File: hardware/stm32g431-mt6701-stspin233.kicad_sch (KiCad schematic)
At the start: 13 parts, among them J101 I2C, J102 UART, J103 CANBUS_IN, J104 CANBUS_OUT, J105 SPI3, J106 CAN TERMINATION, J107 EXT_PWR, J108 MOT_THT, J109 MOT_FPC, U101 SN65HVD230

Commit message: work on layout
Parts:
- removed J103: CANBUS_IN, matei:AVX-009159010061911, symbol Connector_Generic:Conn_01x04
- removed J104: CANBUS_OUT, matei:AVX-009159010061911, symbol Connector_Generic:Conn_01x04
- added H101, H102, H103, H104: M3, MountingHole:MountingHole_3.2mm_M3_DIN965_Pad_TopBottom, symbol Mechanical:MountingHole_Pad
- added J103: CANBUS_IN, matei:AVX-009159010061911, symbol Connector_Generic:Conn_02x05_Top_Bottom
- added J104: CANBUS_OUT, matei:AVX-009159010061911, symbol Connector_Generic:Conn_02x05_Top_Bottom
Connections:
- net +5V: now also J103.8 (Pin_8), J104.3 (Pin_3), J104.4 (Pin_4), J104.8 (Pin_8), J104.9 (Pin_9)
- net CAN_H: now also J103.1 (Pin_1), J103.6 (Pin_6), J104.1 (Pin_1), J104.6 (Pin_6)
- net CAN_L: now also J103.2 (Pin_2), J103.7 (Pin_7), J104.2 (Pin_2), J104.7 (Pin_7)
- net GND: now also H101.1, H102.1, H103.1, H104.1, J103.10 (Pin_10), J103.5 (Pin_5), J104.10 (Pin_10), J104.5 (Pin_5)

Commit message: finalize fab files
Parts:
- removed J108: MOT_THT, Connector_JST:JST_XH_S3B-XH-A_1x03_P2.50mm_Horizontal, symbol Connector_Generic:Conn_01x03
- added J110: MOT_FPC2, matei:FPC-SMD_3P-P1.00_HDGC_1.0K-LS-3PWB-BOTTOMCONTACT, symbol Connector_Generic:Conn_01x03
- H101, H102, H103, H104: footprint MountingHole:MountingHole_3.2mm_M3_DIN965_Pad_TopBottom -> MountingHole:MountingHole_3.2mm_M3_DIN965_Pad
- J101, J102: footprint Connector_PinHeader_2.54mm:PinHeader_1x04_P2.54mm_Vertical -> Connector_PinHeader_2.54mm:PinHeader_2x02_P2.54mm_Vertical
- J105: footprint Connector_PinHeader_2.54mm:PinHeader_1x06_P2.54mm_Vertical -> Connector_PinHeader_2.54mm:PinHeader_2x03_P2.54mm_Vertical
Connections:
- net +5V is gone; now on net Vmot: J101.3 (Pin_3), J102.3 (Pin_3), J103.8 (Pin_8), J104.3 (Pin_3), J104.4 (Pin_4), J104.8 (Pin_8), J104.9 (Pin_9), J105.5 (Pin_5)
- net motor driver/MOT_U: now also J110.3 (Pin_3)
- net motor driver/MOT_V: now also J110.2 (Pin_2)
- net motor driver/MOT_W: now also J110.1 (Pin_1)
- net Vmot: now reaches J103.3 (Pin_3)
- net Vmot: now also J103.4 (Pin_4), J103.9 (Pin_9)
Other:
- note added: "so we can mount FPC in either orientation, for top + bottom"
- moved on the sheet: C101, D?, H101, H102, H103, H104, J101, J102, J103, J104, J105, J106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

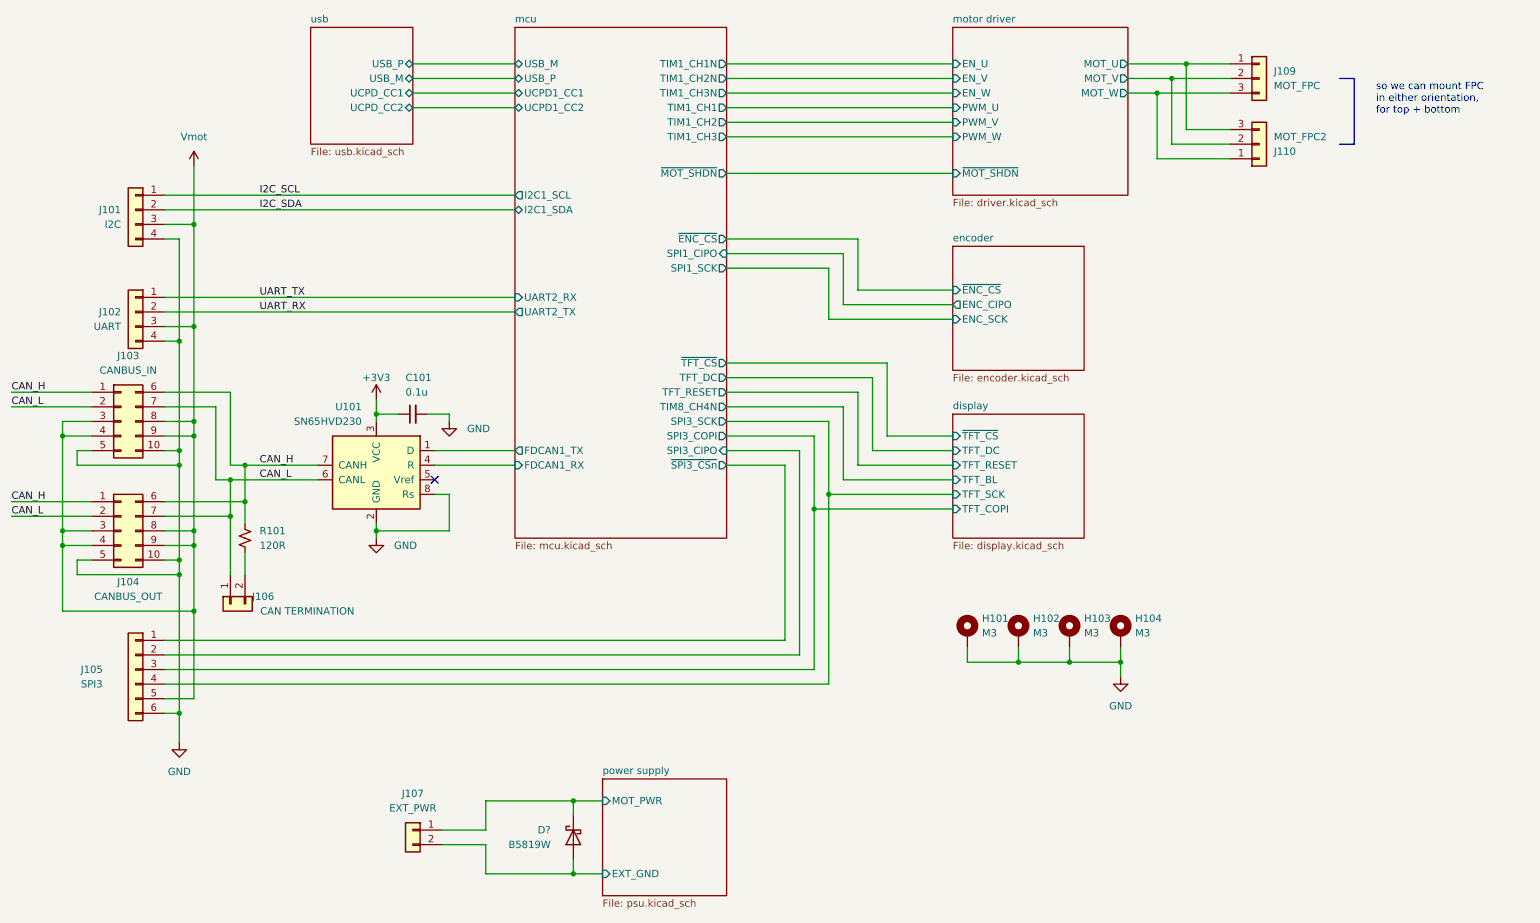
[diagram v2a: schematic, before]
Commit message: update schematic
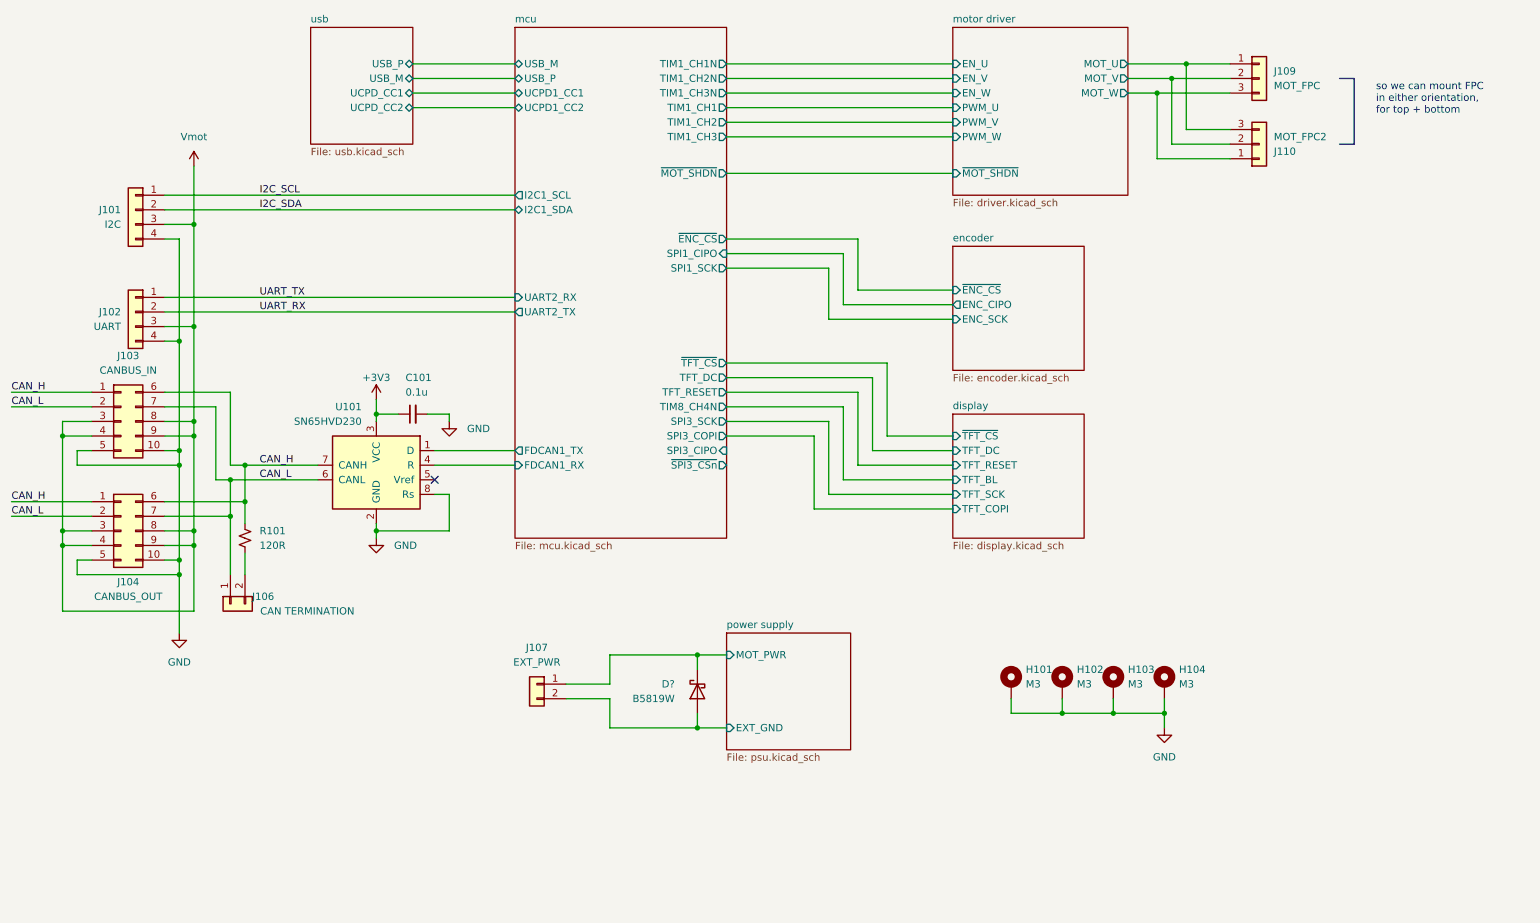
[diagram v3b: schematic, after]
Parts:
- removed J105: SPI3, Connector_PinHeader_2.54mm:PinHeader_2x03_P2.54mm_Vertical, symbol Connector_Generic:Conn_01x06
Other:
- moved on the sheet: D?, H101, H102, H103, H104, J107

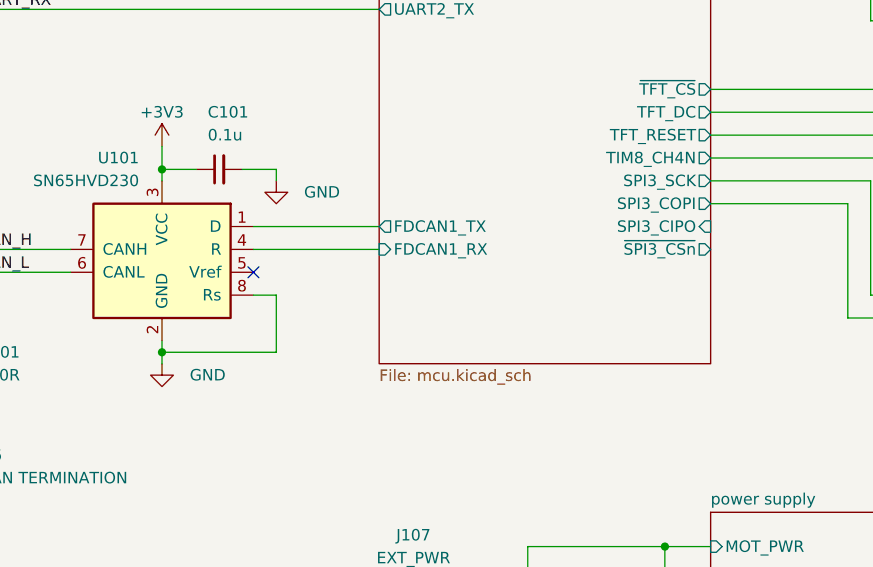
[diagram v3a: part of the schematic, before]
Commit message: update schematic (Vref+ tie to Vdd) and go through ERC check
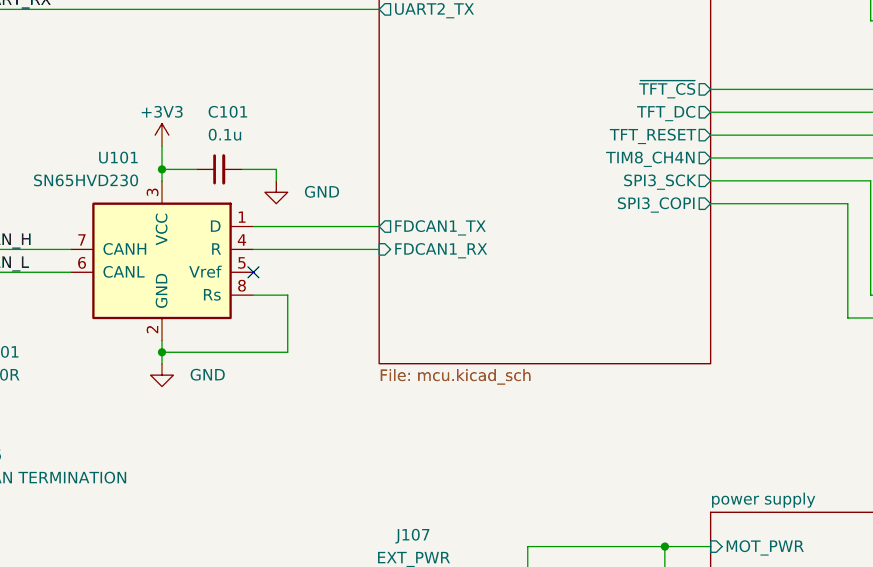
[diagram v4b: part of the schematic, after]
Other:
- sheet mcu ports: added none; removed SPI3_CIPO, ~{SPI3_CSn}
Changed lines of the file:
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@@
   (junction (at 49.53 116.84) (diameter 0) (color 0 0 0 0)
   )
+  (junction (at 81.28 116.84) (diameter 0) (color 0 0 0 0)
+  )
   (junction (at 46.99 105.41) (diameter 0) (color 0 0 0 0)
   )
@@
   )
   (junction (at 49.53 81.28) (diameter 0) (color 0 0 0 0)
-  )
-  (junction (at 81.28 116.84) (diameter 0) (color 0 0 0 0)
   )
   (no_connect (at 91.44 107.95))
@@
     (stroke (width 0) (type default))
   )
-  (wire (pts (xy 81.28 115.57) (xy 81.28 116.84))
-    (stroke (width 0) (type default))
-  )
   (wire (pts (xy 142.24 48.26) (xy 181.61 48.26))
     (stroke (width 0) (type default))
   )
+  (wire (pts (xy 81.28 116.84) (xy 81.28 118.11))
+    (stroke (width 0) (type default))
+  )
   (wire (pts (xy 26.67 100.33) (xy 31.75 100.33))
     (stroke (width 0) (type default))
@@
   )
   (wire (pts (xy 165.1 74.93) (xy 181.61 74.93))
-    (stroke (width 0) (type default))
-  )
-  (wire (pts (xy 91.44 110.49) (xy 93.98 110.49))
     (stroke (width 0) (type default))
   )
@@
     (stroke (width 0) (type default))
   )
-  (wire (pts (xy 93.98 116.84) (xy 81.28 116.84))
-    (stroke (width 0) (type default))
-  )
   (wire (pts (xy 219.71 38.1) (xy 229.87 38.1))
     (stroke (width 0) (type default))
@@
     (stroke (width 0) (type default))
   )
-  (wire (pts (xy 93.98 110.49) (xy 93.98 116.84))
-    (stroke (width 0) (type default))
-  )
   (wire (pts (xy 26.67 130.81) (xy 49.53 130.81))
     (stroke (width 0) (type default))
@@
     (stroke (width 0) (type default))
   )
-  (wire (pts (xy 81.28 116.84) (xy 81.28 118.11))
-    (stroke (width 0) (type default))
-  )
   (wire (pts (xy 142.24 45.72) (xy 181.61 45.72))
     (stroke (width 0) (type default))
@@
     (stroke (width 0) (type default))
   )
+  (wire (pts (xy 95.25 116.84) (xy 81.28 116.84))
+    (stroke (width 0) (type default))
+  )
   (wire (pts (xy 49.53 81.28) (xy 49.53 97.79))
     (stroke (width 0) (type default))
   )
+  (wire (pts (xy 91.44 110.49) (xy 95.25 110.49))
+    (stroke (width 0) (type default))
+  )
   (wire (pts (xy 49.53 97.79) (xy 49.53 100.33))
     (stroke (width 0) (type default))
@@
     (stroke (width 0) (type default))
   )
+  (wire (pts (xy 95.25 110.49) (xy 95.25 116.84))
+    (stroke (width 0) (type default))
+  )
   (wire (pts (xy 55.88 92.71) (xy 55.88 105.41))
     (stroke (width 0) (type default))
@@
   )
   (wire (pts (xy 142.24 95.25) (xy 162.56 95.25))
+    (stroke (width 0) (type default))
+  )
+  (wire (pts (xy 81.28 116.84) (xy 81.28 115.57))
     (stroke (width 0) (type default))
   )
@@
       (effects (font (size 1.27 1.27)) (justify left))
     )
-    (pin "SPI3_CIPO" input (at 142.24 102.87 0)
-      (effects (font (size 1.27 1.27)) (justify right))
-    )
     (pin "SPI3_SCK" output (at 142.24 97.79 0)
       (effects (font (size 1.27 1.27)) (justify right))
@@
       (effects (font (size 1.27 1.27)) (justify right))
     )
-    (pin "~{SPI3_CSn}" output (at 142.24 105.41 0)
-      (effects (font (size 1.27 1.27)) (justify right))
-    )

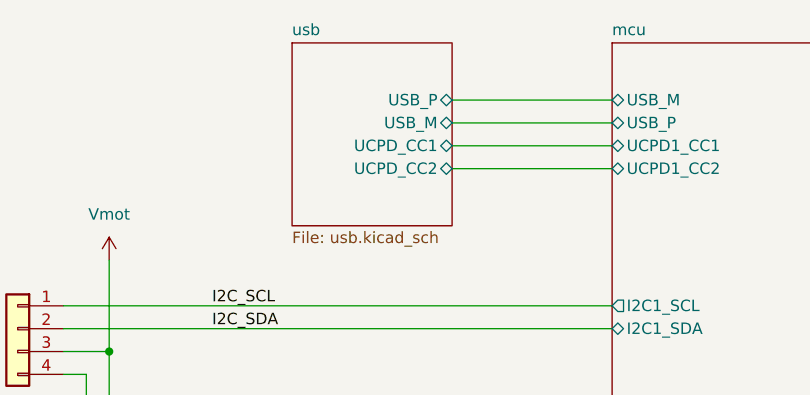
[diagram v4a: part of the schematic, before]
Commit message: Fix swapped USB pins
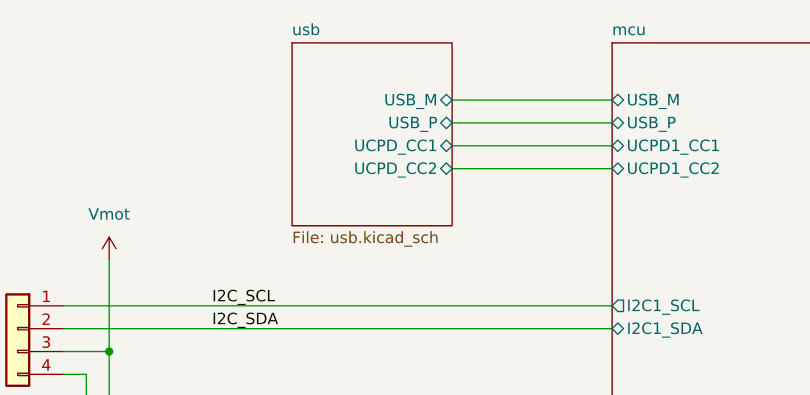
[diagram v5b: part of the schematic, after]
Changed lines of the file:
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@@
       (effects (font (size 1.27 1.27)) (justify right))
     )
-    (pin "USB_M" bidirectional (at 87.63 38.1 0)
+    (pin "USB_M" bidirectional (at 87.63 35.56 0)
       (effects (font (size 1.27 1.27)) (justify right))
     )
-    (pin "USB_P" bidirectional (at 87.63 35.56 0)
+    (pin "USB_P" bidirectional (at 87.63 38.1 0)
       (effects (font (size 1.27 1.27)) (justify right))
     )

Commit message: update schematic to remove debounce cap
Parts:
- H101, H102, H103, H104, J103, J104, J106, J107, J109, J110: now left out of the parts list
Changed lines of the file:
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@@
   )
   (symbol (lib_id "Mechanical:MountingHole_Pad") (at 200.66 143.51 0) (unit 1)
-    (in_bom yes) (on_board yes) (dnp no) (fields_autoplaced)
+    (in_bom no) (on_board yes) (dnp no) (fields_autoplaced)
     (property "Reference" "H102" (at 203.2 140.97 0)
       (effects (font (size 1.27 1.27)) (justify left))
@@
   )
   (symbol (lib_id "Connector_Generic:Conn_01x02") (at 109.22 143.51 0) (mirror y) (unit 1)
-    (in_bom yes) (on_board yes) (dnp no)
+    (in_bom no) (on_board yes) (dnp no)
     (property "Reference" "J107" (at 109.22 137.16 0)
       (effects (font (size 1.27 1.27)))
@@
   )
   (symbol (lib_id "Mechanical:MountingHole_Pad") (at 191.77 143.51 0) (unit 1)
-    (in_bom yes) (on_board yes) (dnp no) (fields_autoplaced)
+    (in_bom no) (on_board yes) (dnp no) (fields_autoplaced)
     (property "Reference" "H101" (at 194.31 140.97 0)
       (effects (font (size 1.27 1.27)) (justify left))
@@
   )
   (symbol (lib_id "Connector_Generic:Conn_02x05_Top_Bottom") (at 36.83 116.84 0) (unit 1)
-    (in_bom yes) (on_board yes) (dnp no)
+    (in_bom no) (on_board yes) (dnp no)
     (property "Reference" "J104" (at 38.1 125.73 0)
       (effects (font (size 1.27 1.27)))
@@
   )
   (symbol (lib_id "Connector_Generic:Conn_01x03") (at 234.95 38.1 0) (unit 1)
-    (in_bom yes) (on_board yes) (dnp no) (fields_autoplaced)
+    (in_bom no) (on_board yes) (dnp no) (fields_autoplaced)
     (property "Reference" "J109" (at 237.49 36.83 0)
       (effects (font (size 1.27 1.27)) (justify left))
@@
   )
   (symbol (lib_id "Mechanical:MountingHole_Pad") (at 209.55 143.51 0) (unit 1)
-    (in_bom yes) (on_board yes) (dnp no) (fields_autoplaced)
+    (in_bom no) (on_board yes) (dnp no) (fields_autoplaced)
     (property "Reference" "H103" (at 212.09 140.97 0)
       (effects (font (size 1.27 1.27)) (justify left))
@@
   )
   (symbol (lib_id "Mechanical:MountingHole_Pad") (at 218.44 143.51 0) (unit 1)
-    (in_bom yes) (on_board yes) (dnp no) (fields_autoplaced)
+    (in_bom no) (on_board yes) (dnp no) (fields_autoplaced)
     (property "Reference" "H104" (at 220.98 140.97 0)
       (effects (font (size 1.27 1.27)) (justify left))
@@
   )
   (symbol (lib_id "Connector_Generic:Conn_01x02") (at 55.88 129.54 90) (mirror x) (unit 1)
-    (in_bom yes) (on_board yes) (dnp no)
+    (in_bom no) (on_board yes) (dnp no)
     (property "Reference" "J106" (at 63.5 128.27 90)
       (effects (font (size 1.27 1.27)) (justify left))
@@
   )
   (symbol (lib_id "Connector_Generic:Conn_01x03") (at 234.95 49.53 0) (mirror x) (unit 1)
-    (in_bom yes) (on_board yes) (dnp no)
+    (in_bom no) (on_board yes) (dnp no)
     (property "Reference" "J110" (at 237.49 50.8 0)
       (effects (font (size 1.27 1.27)) (justify left))
@@
   )
   (symbol (lib_id "Connector_Generic:Conn_02x05_Top_Bottom") (at 36.83 97.79 0) (unit 1)
-    (in_bom yes) (on_board yes) (dnp no) (fields_autoplaced)
+    (in_bom no) (on_board yes) (dnp no) (fields_autoplaced)
     (property "Reference" "J103" (at 38.1 86.36 0)
       (effects (font (size 1.27 1.27)))
